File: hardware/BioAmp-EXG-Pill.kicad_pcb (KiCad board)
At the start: 2 copper layers, 25.4 x 10 mm, 32 parts, among them J1 BioAmp Input, J2 BioAmp Output, U1 TL074

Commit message: BioAmp EXG Pill v1.0 alpha PCB
This version of the BioAmp EXG Pill is near to the final release version (v1.0) for the Crowd Supply campaign.
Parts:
- removed the C7 at (125.7, 91.0)
- added C1: 2.2nF, Capacitor_SMD:C_0603_1608Metric_Pad1.08x0.95mm_HandSolder, F.Cu at (125.7, 91.0)
- C5: renamed from C8; value 2.2uF -> 4.7uF
- C7: renamed from C4; value 2.2uF -> 220nF
- renumbered C5 to C2, C2 to C3, C9 to C4, C1 to C6, J2 to J1, J1 to J2, R6 to R1, R7 to R11, R5 to R12, R8 to R13, R11 to R14, R9 to R15, R13 to R2, R14 to R3, R2 to R4, R4 to R5, R12 to R6, R15 to R7, R1 to R8, R3 to R9
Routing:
- net Net-(R1-Pad2): track 36.2 -> 20.9 mm, vias 4 -> 3
- net IN-: track 6.77 -> 13.4 mm
- net IN+: track 7.03 -> 12.1 mm
- net VCC: track 33.7 -> 37.7 mm, vias 3 -> 4
- net GND: track 25.0 -> 21.6 mm, vias 4 -> 14
- net DRL: track 18.2 -> 21.4 mm
- net ampRef: track 12.2 -> 9.82 mm
- net Net-(R2-Pad1): track 3.59 -> 2.02 mm
- net Net-(R1-Pad1): track 14.8 -> 14.1 mm
- net Net-(C2-Pad1): track 5.58 -> 4.86 mm
- added copper zone on B.Cu, net GND
- added copper zone on F.Cu, net GND
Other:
- board text added: "BANDPASS"
- board text added: "JUNE 2021 - v1.0a"
- board text added: "v1.0a"
- board text removed: "BandPass"
- board text removed: "JUNE 2021 - v0.9"
- board text removed: "v0.9"

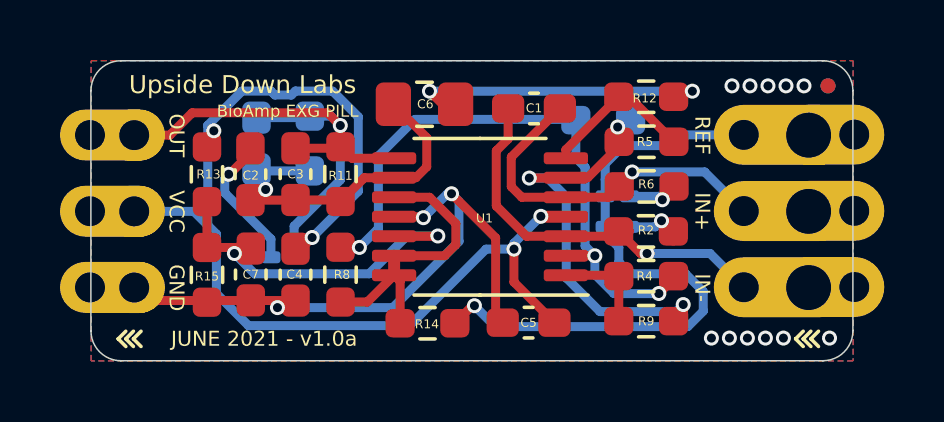
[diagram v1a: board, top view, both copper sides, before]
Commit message: BioAmp EXG Pill v1.0b KiCAD files
This is the Beta version of the BioAmp EXG Pill v1.0 with updated power pinout, solder jumpers and more.
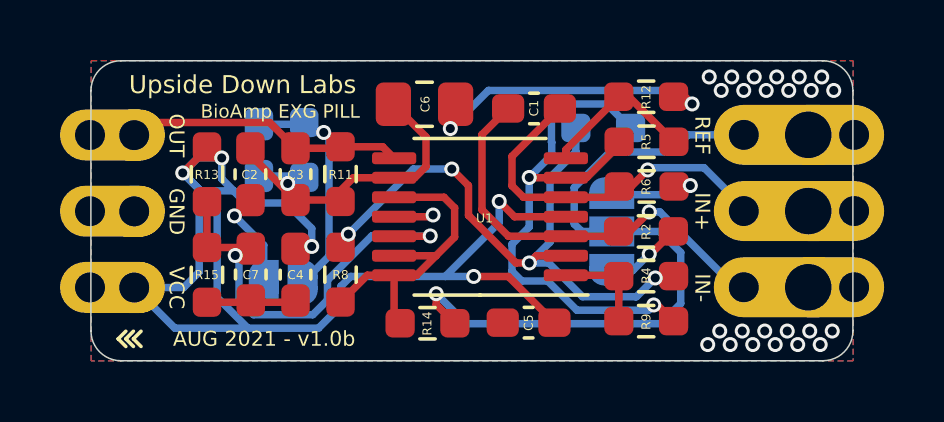
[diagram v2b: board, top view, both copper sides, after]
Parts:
- removed the C3 at (116.5, 92.2)
- removed G***: LOGO, udlabs:EXG
- removed R10, R7: 0R, Resistor_SMD:R_0201_0603Metric_Pad0.64x0.40mm_HandSolder
- removed the R11 at (118.2, 92.2)
- removed REF** (x2): Fiducial_0.5mm_Mask1mm, Fiducial:Fiducial_0.5mm_Mask1mm
- added C8: BPFC_C, Capacitor_SMD:C_0603_1608Metric_Pad1.08x0.95mm_HandSolder, B.Cu at (116.5, 92.4)
- added J2: BioAmp Input, Connector_PinHeader_2.54mm:PinHeader_1x03_P2.54mm_Vertical, F.Cu at (134.8, 91.9)
- added JP1: SolderJumper_3_Open, Jumper:SolderJumper-3_P1.3mm_Open_RoundedPad1.0x1.5mm, B.Cu at (128.3, 95.2)
- added JP2: SolderJumper_2_Open, Jumper:SolderJumper-2_P1.3mm_Open_RoundedPad1.0x1.5mm, B.Cu at (117.3, 96.8)
- added U2: LOGO_UDLABS, udlabs:EXG, B.Cu at (122.2, 94.4)
- R3: value 0R -> BPFC_R; footprint Resistor_SMD:R_0201_0603Metric_Pad0.64x0.40mm_HandSolder -> Resistor_SMD:R_0603_1608Metric_Pad0.98x0.95mm_HandSolder
- moved R3 10.7 mm to (118.0, 92.4), turned to 270 degrees
- moved R1 0.26 mm to (128.0, 91.7)
- turned C2 to 90 degrees
- turned R6 to 0 degrees
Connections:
- C2 pad 2: Net-(C2-Pad2) -> bpfIN
- C3 pad 2: Net-(C2-Pad2) -> bpfIN
- C6 pad 1: Net-(C2-Pad2) -> bpfIN
- J1 pad 2: VCC -> GND (x2)
- J1 pad 3: GND -> VCC (x2)
- R11 pad 2: Net-(C2-Pad2) -> bpfIN
- R2 pad 1: Net-(R2-Pad1) -> Net-(JP1-Pad1)
- R3 pad 1: DRL -> OUT
- R3 pad 2: Net-(R2-Pad1) -> bpfIN
- R6 pad 1: Net-(R6-Pad1) -> IN+
- R6 pad 2: IN+ -> Net-(JP1-Pad3)
- U1 pad 9: Net-(C2-Pad2) -> bpfIN
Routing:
- net GND: track 21.6 -> 4.30 mm, vias 14 -> 25
- net bpfIN: track 0.00 -> 12.8 mm, vias 0 -> 1
- net Net-(C2-Pad2): track 12.2 -> 0.00 mm, vias 1 -> 0
- net VCC: track 37.7 -> 44.4 mm, vias 4 -> 5
- net Net-(R1-Pad1): track 14.1 -> 18.7 mm, vias 3 -> 2
- net Net-(JP1-Pad3): track 0.00 -> 3.33 mm, vias 0 -> 1
- net Net-(JP1-Pad1): track 0.00 -> 2.59 mm, vias 0 -> 1
- net Net-(R2-Pad1): track 2.02 -> 0.00 mm, vias 1 -> 0
- net DRL: track 21.4 -> 23.3 mm, vias 2 -> 1
- net Net-(R6-Pad1): track 1.74 -> 0.00 mm, vias 1 -> 0
- net Net-(C7-Pad1): track 12.7 -> 14.4 mm
- net Net-(C2-Pad1): track 4.86 -> 3.37 mm
- net ampRef: track 9.82 -> 10.9 mm
- net IN-: track 13.4 -> 14.3 mm, vias 2 -> 1
- net Net-(R1-Pad2): track 20.9 -> 21.4 mm, vias 3 -> 4
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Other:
- board text added: "AUG 2021 - v1.0b"
- board text added: "NARROW"
- board text added: "v1.0b"
- board text removed: "3E"
- board text removed: "JUNE 2021 - v1.0a"
- board text removed: "WIDE"
- board text removed: "v1.0a"

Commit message: Update KiCad files v1.0
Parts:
- removed the C2 at (116.3, 93.2)
- added R4: 220K, Resistor_SMD:R_0603_1608Metric_Pad0.98x0.95mm_HandSolder, F.Cu at (116.3, 93.2)
- C2: renamed from C3; value 47nF -> 1nF
- C3: renamed from C7; value 220nF -> 10uF
- C4: renamed from C1; value 2.2nF -> 1nF
- C7: renamed from C5; value 4.7uF -> 10uF
- R10: renamed from R5; value 10K -> 220K
- R11: renamed from R14; value 1k -> 0R
- R2: renamed from R8; value 10K -> 220K
- R5: renamed from R4; value 1K -> 22K
- R7: renamed from R9; value 1K -> 22K
- R8: renamed from R13; value 10K -> 1M
- R9: renamed from R15; value 10K -> 1M
- U1: value TL074 -> Amp
- renumbered C6 to C1, C8 to C5, C4 to C6, JP2 to JP1, JP1 to JP2, R12 to R1, R3 to R12, R2 to R13, R6 to R14, R11 to R3, R1 to R6
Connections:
- net OUT renamed bpfOUT
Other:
- net class Default removed
- board text added: "EMG/ECG"
- board text added: "MAR 2023 - v1.0"
- board text added: "v1.0"
- board text removed: "AUG 2021 - v1.0b"
- board text removed: "NARROW"
- board text removed: "v1.0b"
